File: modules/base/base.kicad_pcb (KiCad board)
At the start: 2 copper layers, 223.5 x 160 mm, 68 parts, among them J2 Ground, J4 Ground, J5 USB_C_Receptacle_PowerOnly_6P, J6 HeadphoneOut, SW1 SW_SPST, U1 AMS1117-3.3, U2 MCP6002-xSN, U3 MCP6002-xSN

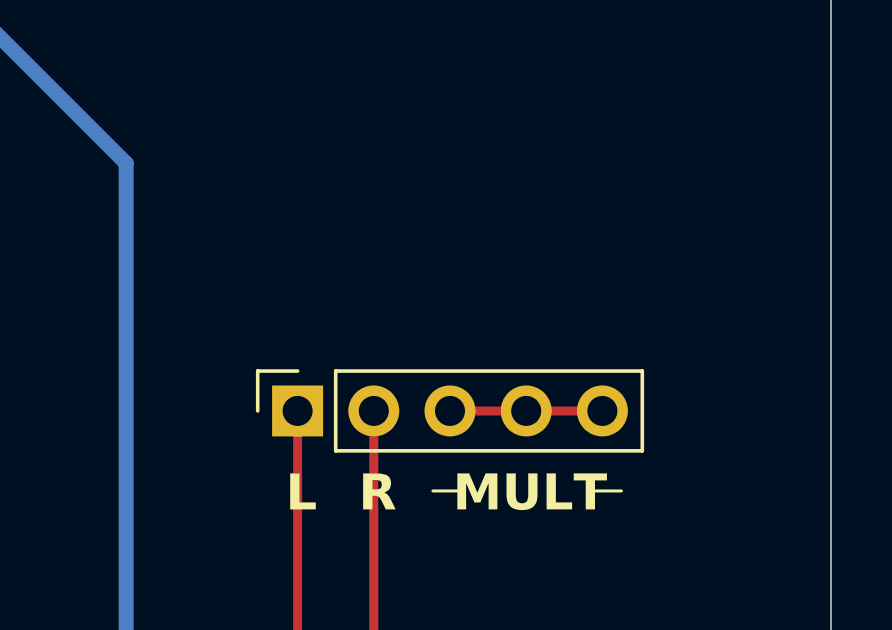
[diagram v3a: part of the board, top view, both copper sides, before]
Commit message: Introduce head_out simulations to base|
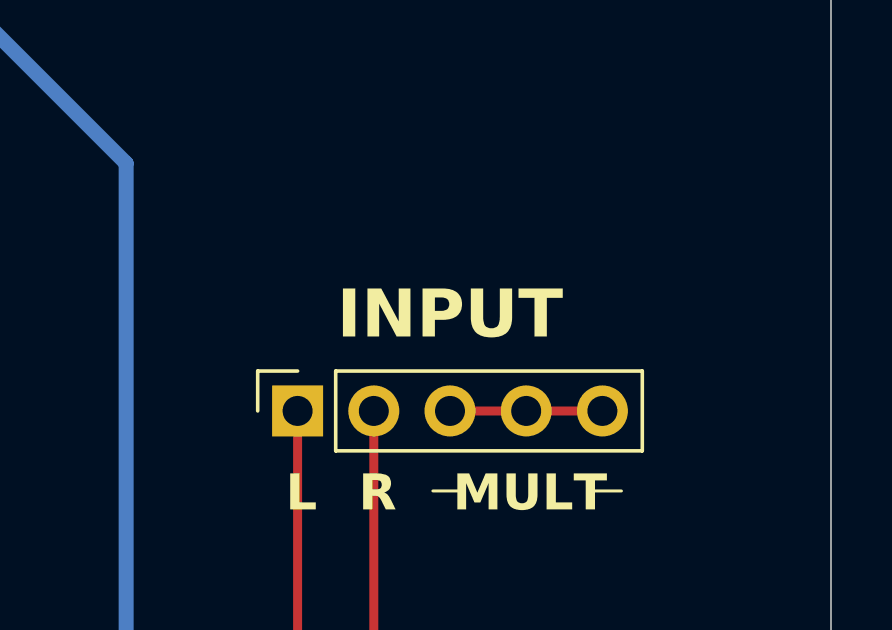
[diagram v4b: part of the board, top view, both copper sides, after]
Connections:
- net Net-(U2A--) renamed BUFF_IN_L
- net Net-(U2B--) renamed BUFF_IN_R
- net OUT_L renamed HEAD_OUT_L
- net OUT_R renamed HEAD_OUT_R
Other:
- board text added: "INPUT"
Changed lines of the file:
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@@
 	(net 22 "Net-(INPUT1-Pin_3)")
 	(net 23 "IN_R")
-	(net 24 "OUT_L")
-	(net 25 "OUT_R")
-	(net 26 "Net-(U2A--)")
+	(net 24 "HEAD_OUT_L")
+	(net 25 "HEAD_OUT_R")
+	(net 26 "BUFF_IN_L")
 	(net 27 "Net-(U3B--)")
 	(net 28 "Net-(R6-Pad1)")
 	(net 29 "Net-(R7-Pad1)")
 	(net 30 "Net-(U3A--)")
-	(net 31 "Net-(U2B--)")
+	(net 31 "BUFF_IN_R")
 	(footprint "Resistor_SMD:R_0402_1005Metric"
 		(layer "F.Cu")
@@
 			(layers "*.Cu" "*.Mask")
 			(remove_unused_layers no)
-			(net 26 "Net-(U2A--)")
+			(net 26 "BUFF_IN_L")
 			(pinfunction "3")
 			(pintype "passive")
@@
 			(remove_unused_layers no)
 			(roundrect_rratio 0.25)
-			(net 25 "OUT_R")
+			(net 25 "HEAD_OUT_R")
 			(pintype "passive")
 		)
@@
 			(remove_unused_layers no)
 			(roundrect_rratio 0.25)
-			(net 24 "OUT_L")
+			(net 24 "HEAD_OUT_L")
 			(pintype "passive")
 		)
@@
 			(layers "F.Cu" "F.Paste" "F.Mask")
 			(roundrect_rratio 0.222222)
-			(net 24 "OUT_L")
+			(net 24 "HEAD_OUT_L")
 			(pintype "passive")
 		)
@@
 			(layers "*.Cu" "*.Mask")
 			(remove_unused_layers no)
-			(net 31 "Net-(U2B--)")
+			(net 31 "BUFF_IN_R")
 			(pinfunction "3")
 			(pintype "passive")
@@
 		)
 		(fp_text user "${REFERENCE}"
-			(at 0 5.08 360)
+			(at 0 5.08 0)
 			(layer "F.Fab")
 			(effects
@@
 			(layers "F.Cu" "F.Paste" "F.Mask")
 			(roundrect_rratio 0.25)
-			(net 26 "Net-(U2A--)")
+			(net 26 "BUFF_IN_L")
 			(pintype "output")
 		)
@@
 			(layers "F.Cu" "F.Paste" "F.Mask")
 			(roundrect_rratio 0.25)
-			(net 26 "Net-(U2A--)")
+			(net 26 "BUFF_IN_L")
 			(pinfunction "-")
 			(pintype "input")
@@
 			(layers "F.Cu" "F.Paste" "F.Mask")
 			(roundrect_rratio 0.25)
-			(net 31 "Net-(U2B--)")
+			(net 31 "BUFF_IN_R")
 			(pinfunction "-")
 			(pintype "input")
@@
 			(layers "F.Cu" "F.Paste" "F.Mask")
 			(roundrect_rratio 0.25)
-			(net 31 "Net-(U2B--)")
+			(net 31 "BUFF_IN_R")
 			(pintype "output")
 		)
@@
 			(layers "F.Cu" "F.Paste" "F.Mask")
 			(roundrect_rratio 0.222222)
-			(net 25 "OUT_R")
+			(net 25 "HEAD_OUT_R")
 			(pintype "passive")
 		)
@@
 			(layers "F.Cu" "F.Paste" "F.Mask")
 			(roundrect_rratio 0.25)
-			(net 26 "Net-(U2A--)")
+			(net 26 "BUFF_IN_L")
 			(pintype "passive")
 		)
@@
 		)
 	)
+	(gr_text "INPUT"
+		(at 241.3 51.054 0)
+		(layer "F.SilkS")
+		(effects
+			(font
+				(size 1.6 1.6)
+				(thickness 0.3)
+				(bold yes)
+			)
+			(justify bottom)
+		)
+	)

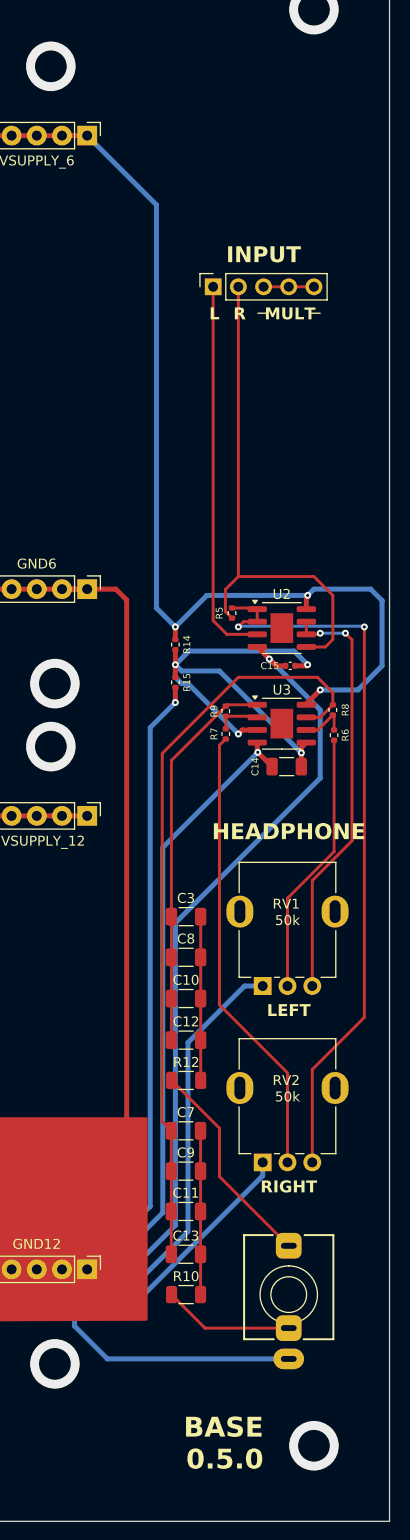
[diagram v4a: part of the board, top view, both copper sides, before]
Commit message: Add line_out into the base
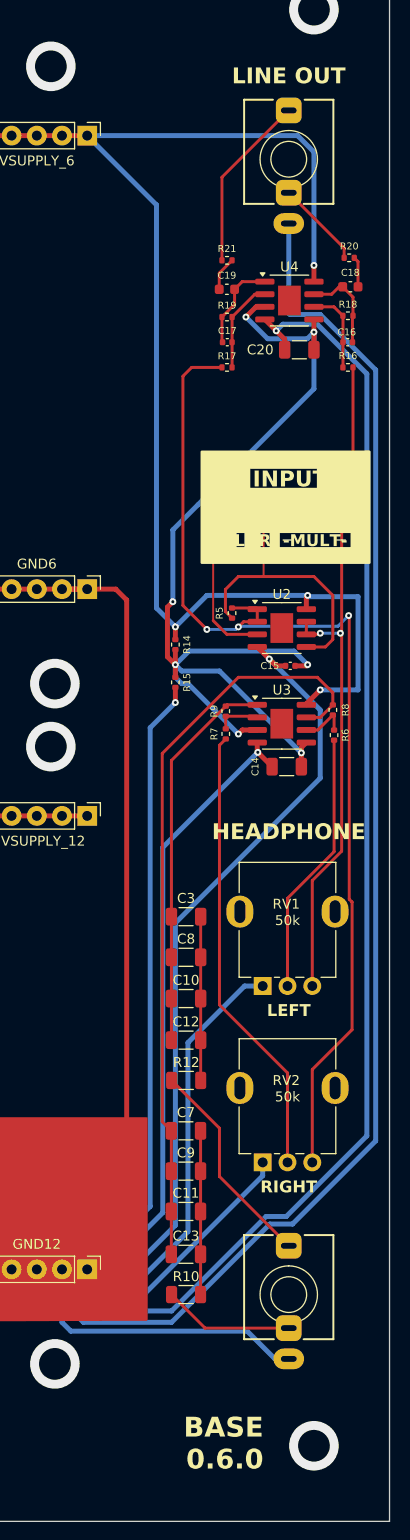
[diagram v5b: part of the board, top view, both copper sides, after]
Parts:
- added C16: 100pf, Capacitor_SMD:C_0402_1005Metric, F.Cu at (249.8, 58.9)
- added C17: 100pf, Capacitor_SMD:C_0402_1005Metric, F.Cu at (237.6, 58.9)
- added C18: 4.7uf, Capacitor_SMD:C_0603_1608Metric, F.Cu at (250.1, 53.3)
- added C19: 4.7uf, Capacitor_SMD:C_0603_1608Metric, F.Cu at (237.6, 53.6)
- added C20: 100uf, Capacitor_SMD:C_1206_3216Metric, F.Cu at (244.9, 59.7)
- added J1: LineOut, BreadModular_AudioJacks:Jack_3.5mm_QingPu_WQP-PJ366ST_Vertical, F.Cu at (243.8, 40.5)
- added R16: 100k, Resistor_SMD:R_0402_1005Metric, F.Cu at (249.8, 61.5)
- added R17: 100k, Resistor_SMD:R_0402_1005Metric, F.Cu at (237.6, 61.5)
- added R18: 33k, Resistor_SMD:R_0402_1005Metric, F.Cu at (249.8, 56.3)
- added R19: 33k, Resistor_SMD:R_0402_1005Metric, F.Cu at (237.6, 56.4)
- added R20: 1k, Resistor_SMD:R_0402_1005Metric, F.Cu at (249.9, 50.4)
- added R21: 1k, Resistor_SMD:R_0402_1005Metric, F.Cu at (237.6, 50.7)
- added U4: MCP6002-xSN, Package_SO:SOIC-8-1EP_3.9x4.9mm_P1.27mm_EP2.29x3mm, F.Cu at (243.9, 54.7)
- moved INPUT1 23.0 mm to (238.8, 76.2)
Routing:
- net GND: track 1103.9 -> 1378.7 mm, vias 65 -> 66
- net +2.5V: track 49.7 -> 103.1 mm, vias 4 -> 7
- net BUFF_IN_L: track 74.9 -> 108.6 mm, vias 2 -> 3
- net +3.3V: track 569.5 -> 602.4 mm, vias 3 -> 4
- net BUFF_IN_R: track 42.8 -> 68.9 mm
- net IN_R: track 52.0 -> 29.1 mm
- net IN_L: track 38.7 -> 16.9 mm
- net LINE_OUT_L: track 0.00 -> 17.9 mm
- net Net-(U4A--): track 0.00 -> 9.34 mm
- net Net-(C17-Pad1): track 0.00 -> 9.26 mm
- net Net-(C16-Pad1): track 0.00 -> 9.25 mm
- net LINE_OUT_R: track 0.00 -> 8.87 mm
- net Net-(U4B--): track 0.00 -> 8.50 mm
- net Net-(C19-Pad2): track 0.00 -> 3.46 mm
- net Net-(C18-Pad2): track 0.00 -> 3.08 mm
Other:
- board text added: "-MULT-"
- board text added: "BASE 0.6.0"
- board text added: "LINE OUT"
- board text removed: "BASE 0.5.0"
- board text removed: "MULT"

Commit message: base: Add input grounding & no buffer on line_out Buffering on the line_out causes noise issues. This fixes it.
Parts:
- removed C16, C17: 100pf, Capacitor_SMD:C_0402_1005Metric
- added R24: 10k, Resistor_SMD:R_0402_1005Metric, F.Cu at (242.4, 64.6)
- added R25: 10k, Resistor_SMD:R_0402_1005Metric, F.Cu at (245.5, 64.6)
- R16, R17: value 100k -> 1M
- R18, R19: value 33k -> 330k
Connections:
- R16 pad 2: BUFF_IN_R -> IN_R
- R17 pad 2: BUFF_IN_L -> IN_L
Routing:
- net GND: track 1378.7 -> 1476.9 mm, vias 66 -> 67
- net BUFF_IN_L: track 108.6 -> 77.8 mm
- net IN_R: track 29.1 -> 58.9 mm
- net BUFF_IN_R: track 68.9 -> 41.6 mm
- net IN_L: track 16.9 -> 39.6 mm
- net +3.3V: track 602.4 -> 612.4 mm
- net Net-(C19-Pad1): track 9.26 -> 6.69 mm
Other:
- board text added: "BASE 0.7.0"
- board text removed: "BASE 0.6.0"

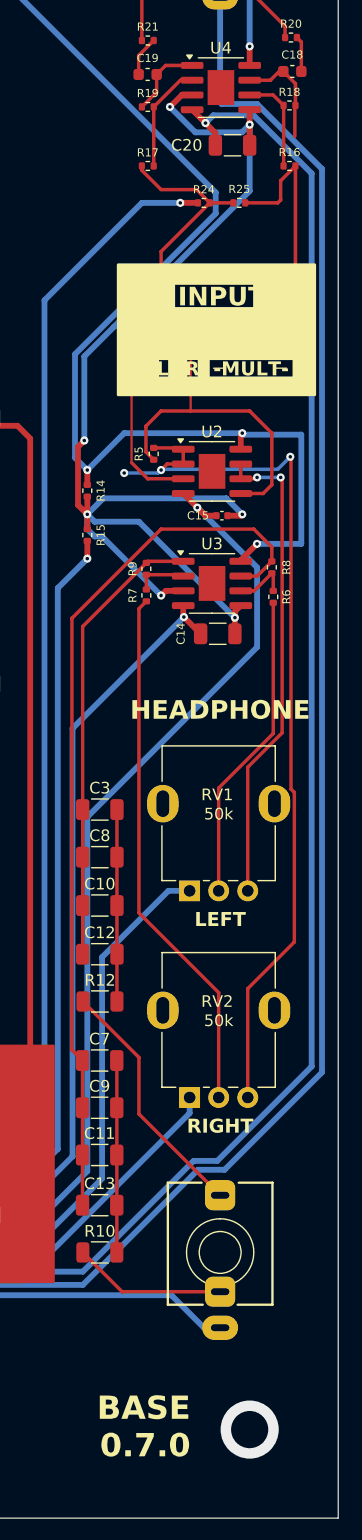
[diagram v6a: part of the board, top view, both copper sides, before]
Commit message: base: update footprint of a resistor
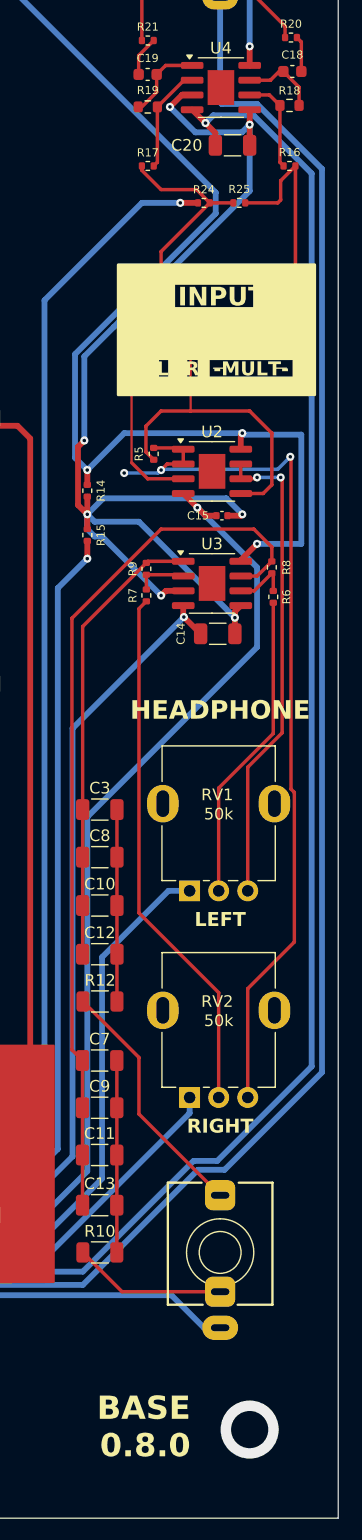
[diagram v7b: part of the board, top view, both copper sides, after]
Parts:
- R18, R19: footprint Resistor_SMD:R_0402_1005Metric -> Resistor_SMD:R_0603_1608Metric
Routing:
- net Net-(C18-Pad1): track 9.25 -> 6.69 mm
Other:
- board text added: "BASE 0.8.0"
- board text removed: "BASE 0.7.0"
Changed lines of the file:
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@@
 		)
 	)
-	(footprint "Resistor_SMD:R_0402_1005Metric"
+	(footprint "Resistor_SMD:R_0603_1608Metric"
 		(layer "F.Cu")
 		(at 237.615 56.388)
-		(descr "Resistor SMD 0402 (1005 Metric), square (rectangular) end terminal, IPC_7351 nominal, (Body size source: IPC-SM-782 page 72, https://www.pcb-3d.com/wordpress/wp-content/uploads/ipc-sm-782a_amendment_1_and_2.pdf), generated with kicad-footprint-generator")
+		(descr "Resistor SMD 0603 (1608 Metric), square (rectangular) end terminal, IPC_7351 nominal, (Body size source: IPC-SM-782 page 72, https://www.pcb-3d.com/wordpress/wp-content/uploads/ipc-sm-782a_amendment_1_and_2.pdf), generated with kicad-footprint-generator")
 		(tags "resistor")
 		(property "Reference" "R19"
-			(at 0 -1.17 0)
+			(at 0 -1.43 0)
 			(layer "F.SilkS")
 			(effects
@@
 		)
 		(property "Value" "330k"
-			(at 0 1.17 0)
+			(at 0 1.43 0)
 			(layer "F.Fab")
 			(effects
@@
 			)
 		)
-		(property "Footprint" "Resistor_SMD:R_0402_1005Metric"
+		(property "Footprint" "Resistor_SMD:R_0603_1608Metric"
 			(at 0 0 0)
 			(unlocked yes)
@@
 		(attr smd)
 		(fp_line
-			(start -0.153641 -0.38)
-			(end 0.153641 -0.38)
+			(start -0.237258 -0.5225)
+			(end 0.237258 -0.5225)
 			(stroke
 				(width 0.12)
@@
 		)
 		(fp_line
-			(start -0.153641 0.38)
-			(end 0.153641 0.38)
+			(start -0.237258 0.5225)
+			(end 0.237258 0.5225)
 			(stroke
 				(width 0.12)
@@
 		)
 		(fp_line
-			(start -0.93 -0.47)
-			(end 0.93 -0.47)
+			(start -1.48 -0.73)
+			(end 1.48 -0.73)
 			(stroke
 				(width 0.05)
@@
 		)
 		(fp_line
-			(start -0.93 0.47)
-			(end -0.93 -0.47)
+			(start -1.48 0.73)
+			(end -1.48 -0.73)
 			(stroke
 				(width 0.05)
@@
 		)
 		(fp_line
-			(start 0.93 -0.47)
-			(end 0.93 0.47)
+			(start 1.48 -0.73)
+			(end 1.48 0.73)
 			(stroke
 				(width 0.05)
@@
 		)
 		(fp_line
-			(start 0.93 0.47)
-			(end -0.93 0.47)
+			(start 1.48 0.73)
+			(end -1.48 0.73)
 			(stroke
 				(width 0.05)
@@
 		)
 		(fp_line
-			(start -0.525 -0.27)
-			(end 0.525 -0.27)
+			(start -0.8 -0.4125)
+			(end 0.8 -0.4125)
 			(stroke
 				(width 0.1)
@@
 		)
 		(fp_line
-			(start -0.525 0.27)
-			(end -0.525 -0.27)
+			(start -0.8 0.4125)
+			(end -0.8 -0.4125)
 			(stroke
 				(width 0.1)
@@
 		)
 		(fp_line
-			(start 0.525 -0.27)
-			(end 0.525 0.27)
+			(start 0.8 -0.4125)
+			(end 0.8 0.4125)
 			(stroke
 				(width 0.1)
@@
 		)
 		(fp_line
-			(start 0.525 0.27)
-			(end -0.525 0.27)
+			(start 0.8 0.4125)
+			(end -0.8 0.4125)
 			(stroke
 				(width 0.1)
@@
 			(effects
 				(font
-					(size 0.26 0.26)
-					(thickness 0.04)
+					(size 0.4 0.4)
+					(thickness 0.06)
 				)
 			)
 		)
 		(pad "1" smd roundrect
-			(at -0.51 0)
-			(size 0.54 0.64)
+			(at -0.825 0)
+			(size 0.8 0.95)
 			(layers "F.Cu" "F.Paste" "F.Mask")
 			(roundrect_rratio 0.25)
@@
 		)
 		(pad "2" smd roundrect
-			(at 0.51 0)
-			(size 0.54 0.64)
+			(at 0.825 0)
+			(size 0.8 0.95)
 			(layers "F.Cu" "F.Paste" "F.Mask")
 			(roundrect_rratio 0.25)
@@
 			(pintype "passive")
 		)
-		(model "${KICAD8_3DMODEL_DIR}/Resistor_SMD.3dshapes/R_0402_1005Metric.wrl"
+		(model "${KICAD8_3DMODEL_DIR}/Resistor_SMD.3dshapes/R_0603_1608Metric.wrl"
 			(offset
 				(xyz 0 0 0)
@@
 		)
 	)
-	(footprint "Resistor_SMD:R_0402_1005Metric"
+	(footprint "Resistor_SMD:R_0603_1608Metric"
 		(layer "F.Cu")
 		(at 249.807 56.261 180)
-		(descr "Resistor SMD 0402 (1005 Metric), square (rectangular) end terminal, IPC_7351 nominal, (Body size source: IPC-SM-782 page 72, https://www.pcb-3d.com/wordpress/wp-content/uploads/ipc-sm-782a_amendment_1_and_2.pdf), generated with kicad-footprint-generator")
+		(descr "Resistor SMD 0603 (1608 Metric), square (rectangular) end terminal, IPC_7351 nominal, (Body size source: IPC-SM-782 page 72, https://www.pcb-3d.com/wordpress/wp-content/uploads/ipc-sm-782a_amendment_1_and_2.pdf), generated with kicad-footprint-generator")
 		(tags "resistor")
 		(property "Reference" "R18"
-			(at 0 1.143 0)
+			(at 0 1.27 180)
 			(layer "F.SilkS")
 			(effects
@@
 		)
 		(property "Value" "330k"
-			(at 0 1.17 0)
+			(at 0 1.43 180)
 			(layer "F.Fab")
 			(effects
@@
 			)
 		)
-		(property "Footprint" "Resistor_SMD:R_0402_1005Metric"
+		(property "Footprint" "Resistor_SMD:R_0603_1608Metric"
 			(at 0 0 180)
 			(unlocked yes)
@@
 		(attr smd)
 		(fp_line
-			(start -0.153641 0.38)
-			(end 0.153641 0.38)
+			(start -0.237258 0.5225)
+			(end 0.237258 0.5225)
 			(stroke
 				(width 0.12)
@@
 		)
 		(fp_line
-			(start -0.153641 -0.38)
-			(end 0.153641 -0.38)
+			(start -0.237258 -0.5225)
+			(end 0.237258 -0.5225)
 			(stroke
 				(width 0.12)
@@
 		)
 		(fp_line
-			(start 0.93 0.47)
-			(end -0.93 0.47)
+			(start 1.48 0.73)
+			(end -1.48 0.73)
 			(stroke
 				(width 0.05)
@@
 		)
 		(fp_line
-			(start 0.93 -0.47)
-			(end 0.93 0.47)
+			(start 1.48 -0.73)
+			(end 1.48 0.73)
 			(stroke
 				(width 0.05)
@@
 		)
 		(fp_line
-			(start -0.93 0.47)
-			(end -0.93 -0.47)
+			(start -1.48 0.73)
+			(end -1.48 -0.73)
 			(stroke
 				(width 0.05)
@@
 		)
 		(fp_line
-			(start -0.93 -0.47)
-			(end 0.93 -0.47)
+			(start -1.48 -0.73)
+			(end 1.48 -0.73)
 			(stroke
 				(width 0.05)
@@
 		)
 		(fp_line
-			(start 0.525 0.27)
-			(end -0.525 0.27)
+			(start 0.8 0.4125)
+			(end -0.8 0.4125)
 			(stroke
 				(width 0.1)
@@
 		)
 		(fp_line
-			(start 0.525 -0.27)
-			(end 0.525 0.27)
+			(start 0.8 -0.4125)
+			(end 0.8 0.4125)
 			(stroke
 				(width 0.1)
@@
 		)
 		(fp_line
-			(start -0.525 0.27)
-			(end -0.525 -0.27)
+			(start -0.8 0.4125)
+			(end -0.8 -0.4125)
 			(stroke
 				(width 0.1)
@@
 		)
 		(fp_line
-			(start -0.525 -0.27)
-			(end 0.525 -0.27)
+			(start -0.8 -0.4125)
+			(end 0.8 -0.4125)
 			(stroke
 				(width 0.1)
@@
 		)
 		(fp_text user "${REFERENCE}"
-			(at 0 0 0)
+			(at 0 0 180)
 			(layer "F.Fab")
 			(effects
 				(font
-					(size 0.26 0.26)
-					(thickness 0.04)
+					(size 0.4 0.4)
+					(thickness 0.06)
 				)
 			)
 		)
 		(pad "1" smd roundrect
-			(at -0.51 0 180)
-			(size 0.54 0.64)
+			(at -0.825 0 180)
+			(size 0.8 0.95)
 			(layers "F.Cu" "F.Paste" "F.Mask")
 			(roundrect_rratio 0.25)
@@
 		)
 		(pad "2" smd roundrect
-			(at 0.51 0 180)
-			(size 0.54 0.64)
+			(at 0.825 0 180)
+			(size 0.8 0.95)
 			(layers "F.Cu" "F.Paste" "F.Mask")
 			(roundrect_rratio 0.25)
@@
 			(pintype "passive")
 		)
-		(model "${KICAD8_3DMODEL_DIR}/Resistor_SMD.3dshapes/R_0402_1005Metric.wrl"
+		(model "${KICAD8_3DMODEL_DIR}/Resistor_SMD.3dshapes/R_0603_1608Metric.wrl"
 			(offset
 				(xyz 0 0 0)
@@
 		)
 	)
-	(gr_text "BASE\n0.7.0"
+	(gr_text "BASE\n0.8.0"
 		(at 241.3 172.72 0)
 		(layer "F.SilkS")
@@
 	)
 	(segment
-		(start 249.304 61.461)
-		(end 249.297 61.468)
-		(width 0.3)
-		(layer "F.Cu")
-		(net 32)
-	)
-	(segment
-		(start 249.304 58.928)
-		(end 249.304 61.461)
+		(start 248.081 55.36)
+		(end 248.982 56.261)
 		(width 0.3)
 		(layer "F.Cu")
@@
 	)
 	(segment
-		(start 248.396 55.36)
-		(end 246.38 55.36)
-		(width 0.3)
-		(layer "F.Cu")
-		(net 32)
-	)
-	(segment
-		(start 249.304 58.928)
-		(end 249.304 56.268)
+		(start 248.982 61.153)
+		(end 249.297 61.468)
 		(width 0.3)
 		(layer "F.Cu")
@@
 	)
 	(segment
-		(start 249.297 56.261)
-		(end 248.396 55.36)
+		(start 246.38 55.36)
+		(end 248.081 55.36)
 		(width 0.3)
 		(layer "F.Cu")
@@
 	)
 	(segment
-		(start 249.304 56.268)
-		(end 249.297 56.261)
+		(start 248.982 56.261)
+		(end 248.982 61.153)
 		(width 0.3)
 		(layer "F.Cu")
@@
 	)
 	(segment
-		(start 250.264 58.928)
-		(end 250.264 56.314)
-		(width 0.3)
-		(layer "F.Cu")
-		(net 33)
-	)
-	(segment
 		(start 248.92 53.34)
 		(end 248.17 54.09)
@@
 	)
 	(segment
-		(start 250.317 54.382)
-		(end 249.275 53.34)
+		(start 250.632 56.261)
+		(end 250.632 54.697)
 		(width 0.3)
 		(layer "F.Cu")
@@
 	)
 	(segment
-		(start 250.317 56.261)
-		(end 250.317 54.382)
-		(width 0.3)
-		(layer "F.Cu")
-		(net 33)
-	)
-	(segment
-		(start 250.264 56.314)
-		(end 250.317 56.261)
+		(start 250.632 54.697)
+		(end 249.275 53.34)
 		(width 0.3)
 		(layer "F.Cu")
@@
 	)
 	(segment
-		(start 241.43 54.09)
-		(end 240.423 54.09)
+		(start 240.738 54.09)
+		(end 241.43 54.09)
 		(width 0.3)
 		(layer "F.Cu")
@@
 	)
 	(segment
-		(start 240.423 54.09)
-		(end 238.125 56.388)
+		(start 238.44 61.153)
+		(end 238.125 61.468)
 		(width 0.3)
 		(layer "F.Cu")
@@
 	)
 	(segment
-		(start 238.125 56.388)
-		(end 238.125 58.928)
+		(start 238.44 56.388)
+		(end 238.44 61.153)
 		(width 0.3)
 		(layer "F.Cu")
@@
 	)
 	(segment
-		(start 238.125 61.468)
-		(end 238.125 58.928)
+		(start 238.44 56.388)
+		(end 240.738 54.09)
 		(width 0.3)
 		(layer "F.Cu")

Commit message: base_1.0.0
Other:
- board text added: "BASE 1.0.0"
- board text removed: "BASE 0.8.0"
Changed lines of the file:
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@@
 		)
 	)
-	(gr_text "BASE\n0.8.0"
+	(gr_text "BASE\n1.0.0"
 		(at 241.3 172.72 0)
 		(layer "F.SilkS")
